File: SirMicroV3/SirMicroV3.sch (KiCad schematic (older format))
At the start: 46 parts, among them J1 Conn_01x17, J2 Conn_01x17, J3 SirBlue, J4 Conn_02x03_Odd_Even, P1 USB_C_Plug_USB2.0, U1 ATmega32U4-MU, U2 SPX3819M5-L-3-3, Y1 20MHz

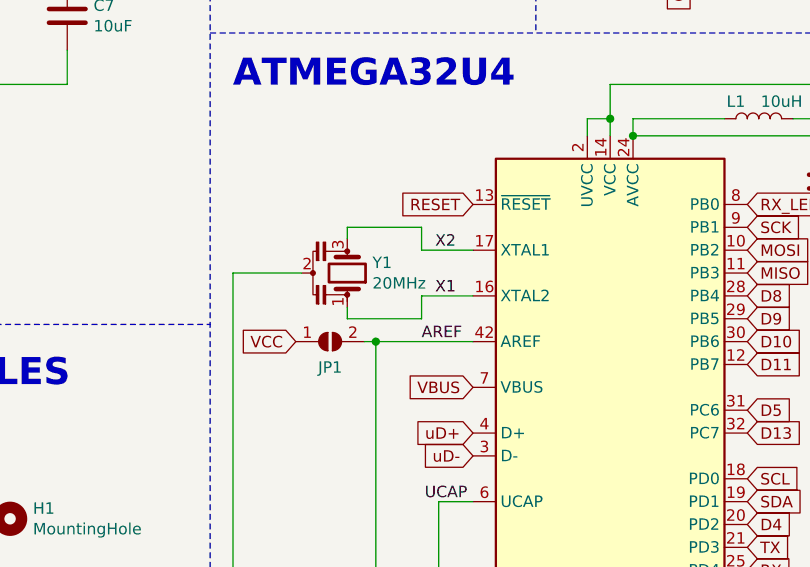
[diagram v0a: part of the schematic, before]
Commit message: Schematic Update - SirMicroR3
20Mhz Changed to 16Mhz
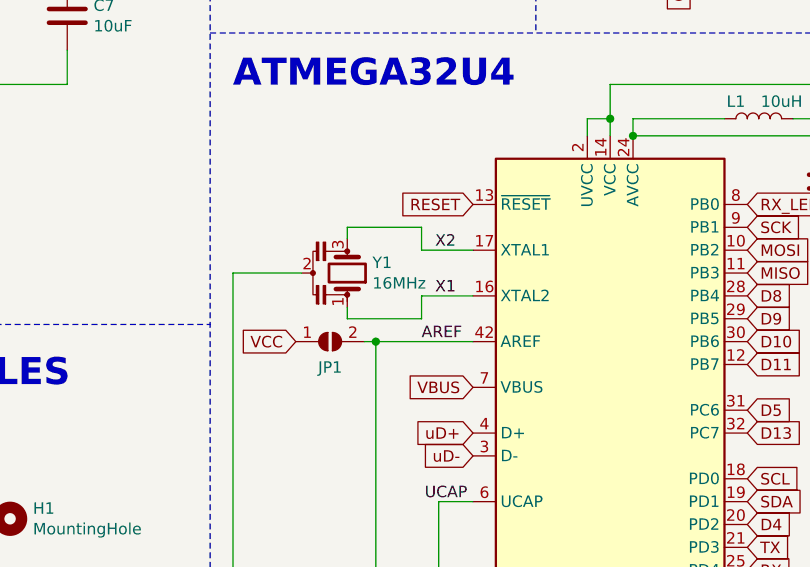
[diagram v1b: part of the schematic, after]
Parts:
- U2: Part (none) -> C9055
- Y1: value 20MHz -> 16MHz; Part C91586 -> C32180
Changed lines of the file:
@@
 P 7725 3075
 F 0 "Y1" V 7770 3185 50  0000 L CNN
-F 1 "20MHz" V 7680 3185 50  0000 L CNN
+F 1 "16MHz" V 7680 3185 50  0000 L CNN
 F 2 "Crystal:Resonator_SMD_muRata_CSTxExxV-3Pin_3.0x1.1mm" H 7700 3075 50  0001 C CNN
 F 3 "~" H 7700 3075 50  0001 C CNN
-F 4 "C91586" V 7725 3075 50  0001 C CNN "Part"
+F 4 "C32180" V 7725 3075 50  0001 C CNN "Part"
 	1    7725 3075
 	0    1    -1   0
@@
 F 1 "SPX3819M5-L-3-3" H 5750 1950 50  0000 C CNN
 F 2 "Package_TO_SOT_SMD:SOT-23-5" H 5750 2025 50  0001 C CNN
-F 3 "https://www.exar.com/content/document.ashx?id=22106&languageid=1033&type=Datasheet&partnumber=SPX3819&filename=SPX3819.pdf&part=SPX3819" H 5750 1700 50  0001 C CNN
+F 3 "https://lcsc.com/product-detail/Low-Dropout-Regulators-LDO_Exar-SPX3819M5-L-3-3-TR_C9055.html" H 5750 1700 50  0001 C CNN
+F 4 "C9055" H 5750 1700 50  0001 C CNN "Part"
 	1    5750 1700
 	1    0    0    -1
